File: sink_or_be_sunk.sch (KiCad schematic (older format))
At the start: 57 parts, among them J1 Keypad_Conn, J2 Mux_Conn, J3 Display_Conn, J4 JTAG_Conn, J5 Battery_Conn, J6 USB_B_Micro, J7 Debug_Conn, M1 Motor_DC, Q1 IRLML5203, Q2 2N3704, Q3 2N3704, Q4 Q_PMOS_DGS, SW1 Reset_SW, SW2 SW_DPST, U1 SN74HC151N, U2 LDL1117-SMD, U3 MCP73831-2-OT, U4 MCP608, U5 ESP32-WROOM-32, U6 CY7C65213A-28PVXI

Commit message: finished routing power and programming circuit
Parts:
- removed H2: MountingHole, MountingHole:MountingHole_3.2mm_M3, symbol Mechanical:MountingHole
- removed R? (x2): 20, symbol Device:R
- added H2: ESP_GND_Pad_Hole, MountingHole:MountingHole_2.2mm_M2_DIN965_Pad, symbol Mechanical:MountingHole_Pad
- added H5: Mounting, MountingHole:MountingHole_3.2mm_M3, symbol Mechanical:MountingHole
- added J10, J11, J12, J13, J14, J15, J16, J17, J18, J19, J20, J21, J22, J23, J9: Grid_Conn, Connector_PinSocket_2.54mm:PinSocket_1x06_P2.54mm_Vertical, symbol Connector:Conn_01x06_Female
- added J8: Grid_Conn_LED, Connector_PinSocket_2.54mm:PinSocket_1x07_P2.54mm_Vertical, symbol Connector:Conn_01x07_Female
- added R10, R14, R15, R16, R17, R18, R19, R20, R21, R22, R23, R24, R25, R26, R9: 20, Resistor_SMD:R_0805_2012Metric_Pad1.20x1.40mm_HandSolder, symbol Device:R
- C1, C2, C3, C4: footprint Capacitor_SMD:C_0805_2012Metric_Pad1.18x1.45mm_HandSolder -> Capacitor_THT:CP_Radial_D4.0mm_P2.00mm
- C12: footprint Capacitor_THT:CP_Radial_D8.0mm_P3.50mm -> Capacitor_THT:CP_Radial_D4.0mm_P2.00mm
- C7: value 100uF -> 10uF; footprint Capacitor_THT:CP_Radial_D8.0mm_P3.50mm -> Capacitor_THT:CP_Radial_D4.0mm_P2.00mm
- D2, D5: footprint Diode_THT:D_DO-15_P10.16mm_Horizontal -> Diode_THT:D_A-405_P7.62mm_Horizontal
- H1, H3, H4: value MountingHole -> Mounting
- Q1: value IRLML5203 -> IRL530; symbol Transistor_FET:IRLML5203 -> Device:Q_NMOS_GDS
- Q4: footprint Package_TO_SOT_THT:TO-220-3_Vertical -> Package_TO_SOT_THT:TO-220-3_Horizontal_TabDown
- R13: renamed from R?; footprint Resistor_SMD:R_0805_2012Metric_Pad1.15x1.40mm_HandSolder -> Resistor_SMD:R_0805_2012Metric_Pad1.20x1.40mm_HandSolder
- TP1, TP2: footprint TestPoint:TestPoint_Pad_2.0x2.0mm -> TestPoint:TestPoint_Plated_Hole_D2.0mm
- gave numbers to parts that had none: 1
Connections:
- net DAC_OUT is gone; now on net SPEAKER: U4.2
- net +3V3: now also J10.1 (Pin_1), J11.1 (Pin_1), J12.1 (Pin_1), J13.1 (Pin_1), J14.1 (Pin_1), J15.1 (Pin_1), J16.1 (Pin_1), J17.1 (Pin_1), J18.1 (Pin_1), J19.1 (Pin_1), J20.1 (Pin_1), J21.1 (Pin_1), J22.1 (Pin_1), J23.1 (Pin_1), J8.1 (Pin_1), J9.1 (Pin_1)
- net +BATT: now also SW2.1; no longer SW2.3
- net BOAT_INPUT: now also J10.5 (Pin_5), J11.5 (Pin_5), J12.5 (Pin_5), J13.5 (Pin_5), J14.5 (Pin_5), J15.5 (Pin_5), J16.5 (Pin_5), J17.5 (Pin_5), J18.5 (Pin_5), J19.5 (Pin_5), J20.5 (Pin_5), J21.5 (Pin_5), J22.5 (Pin_5), J23.5 (Pin_5), J8.5 (Pin_5), J9.5 (Pin_5)
- net GND: now also Q1.3 (S), SW2.3, H2.1, J10.6 (Pin_6), J11.6 (Pin_6), J12.6 (Pin_6), J13.6 (Pin_6), J14.6 (Pin_6), J15.6 (Pin_6), J16.6 (Pin_6), J17.6 (Pin_6), J18.6 (Pin_6), J19.6 (Pin_6), J20.6 (Pin_6), J21.6 (Pin_6), J22.6 (Pin_6), J23.6 (Pin_6), J8.7 (Pin_7), J9.6 (Pin_6); no longer Q1.2 (S), SW2.1
- net LCD_CS: now also R19.1; no longer J3.4 (Pin_4)
- net LCD_MOSI: now also R21.1; no longer J3.2 (Pin_2)
- net LCD_SCLK: now also R20.1; no longer J3.3 (Pin_3)
- net LED_OUT: now also J8.6 (Pin_6)
- net MTCK: now also R24.1; no longer J4.3 (Pin_3)
- net MTDI: now also R25.1; no longer J4.2 (Pin_2)
- net MTDO: now also R22.1
- net MTMS: now also R26.1; no longer J4.1 (Pin_1)
- net MUX_COL_SEL0: now also J10.4 (Pin_4), J11.4 (Pin_4), J12.4 (Pin_4), J13.4 (Pin_4), J14.4 (Pin_4), J15.4 (Pin_4), J16.4 (Pin_4), J17.4 (Pin_4), J18.4 (Pin_4), J19.4 (Pin_4), J20.4 (Pin_4), J21.4 (Pin_4), J22.4 (Pin_4), J23.4 (Pin_4), J8.4 (Pin_4), J9.4 (Pin_4)
- net MUX_COL_SEL1: now also J10.2 (Pin_2), J11.2 (Pin_2), J12.2 (Pin_2), J13.2 (Pin_2), J14.2 (Pin_2), J15.2 (Pin_2), J16.2 (Pin_2), J17.2 (Pin_2), J18.2 (Pin_2), J19.2 (Pin_2), J20.2 (Pin_2), J21.2 (Pin_2), J22.2 (Pin_2), J23.2 (Pin_2), J8.2 (Pin_2), J9.2 (Pin_2)
- net MUX_COL_SEL2: now also J10.3 (Pin_3), J11.3 (Pin_3), J12.3 (Pin_3), J13.3 (Pin_3), J14.3 (Pin_3), J15.3 (Pin_3), J16.3 (Pin_3), J17.3 (Pin_3), J18.3 (Pin_3), J19.3 (Pin_3), J20.3 (Pin_3), J21.3 (Pin_3), J22.3 (Pin_3), J23.3 (Pin_3), J8.3 (Pin_3), J9.3 (Pin_3)
- net MUX_ROW0: now also R15.1; no longer J2.4 (Pin_4)
- net MUX_ROW1: now also R14.1; no longer J2.3 (Pin_3)
- net MUX_ROW2: now also R10.1; no longer J2.2 (Pin_2)
- net MUX_ROW3: now also R9.1; no longer J2.1 (Pin_1)
- net MUX_ROW4: now also R16.1; no longer J2.5 (Pin_5)
- net MUX_ROW5: now also R17.1; no longer J2.6 (Pin_6)
- net MUX_ROW6: now also R18.1; no longer J2.7 (Pin_7)
- net MUX_ROW7: now also R23.1; no longer J2.8 (Pin_8)
- net VBUS: no longer C1.1
- net at J4.4 (Pin_4): now also R22.2
- net at SW2.2: now also J5.2 (Pin_2); no longer J5.1 (Pin_1)
- net at SW2.4: now also J5.1 (Pin_1); no longer J5.2 (Pin_2)
- net at D2.2 (A), M1.2 (-): now also Q1.2 (D); no longer Q1.3 (D)
- net Vin: now reaches D5.1 (K), Q4.3 (S), U2.3 (VIN)
- net Vin: now also C1.1
- net SENSOR_VN: no longer names the net of U5.5 (SENSOR_VN)
- net SENSOR_VP: no longer names the net of U5.4 (SENSOR_VP)
- new net: J4.1 (Pin_1), R26.2
- new net: J4.2 (Pin_2), R25.2
- new net: J4.3 (Pin_3), R24.2
- new net: J2.1 (Pin_1), R9.2
- new net: J2.2 (Pin_2), R10.2
- new net: J2.3 (Pin_3), R14.2
- new net: J2.4 (Pin_4), R15.2
- new net: J2.5 (Pin_5), R16.2
- new net: J2.6 (Pin_6), R17.2
- new net: J2.7 (Pin_7), R18.2
- new net: J2.8 (Pin_8), R23.2
- new net: J3.2 (Pin_2), R21.2
- new net: J3.3 (Pin_3), R20.2
- new net: J3.4 (Pin_4), R19.2
- no-connect marks 14 -> 16
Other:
- note added: "R for ESD Protection\n"
- note added: "Speaker/Amplifier"
- note added: "TODO: \n- heat calcs for LDO, MOSFET in Power and filtering section, speaker\n- measure bulk capacitor for diameter(footprints)"
- note removed: "Big Via for pad 39 GND on Esp module for soldering"
- note removed: "Decoupling/Bulk Caps"
- note removed: "Mounting Holes"
- note removed: "R for\nESD Protection\n"
- note removed: "Reset"
- note removed: "TODO: \n- 20 ohm for JTAG, MUX\n- connectors for all 16 grid boards\n- big via for gnd pad on esp\n- heat calcs for LDO, MOSFET in Power and filtering section, speaker\n- test speaker circuit for sound volume"
- note removed: "need headers to Grid PCB"
- moved on the sheet: C1, C10, C11, C12, C2, C3, C4, C5, C6, C7, C8, C9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

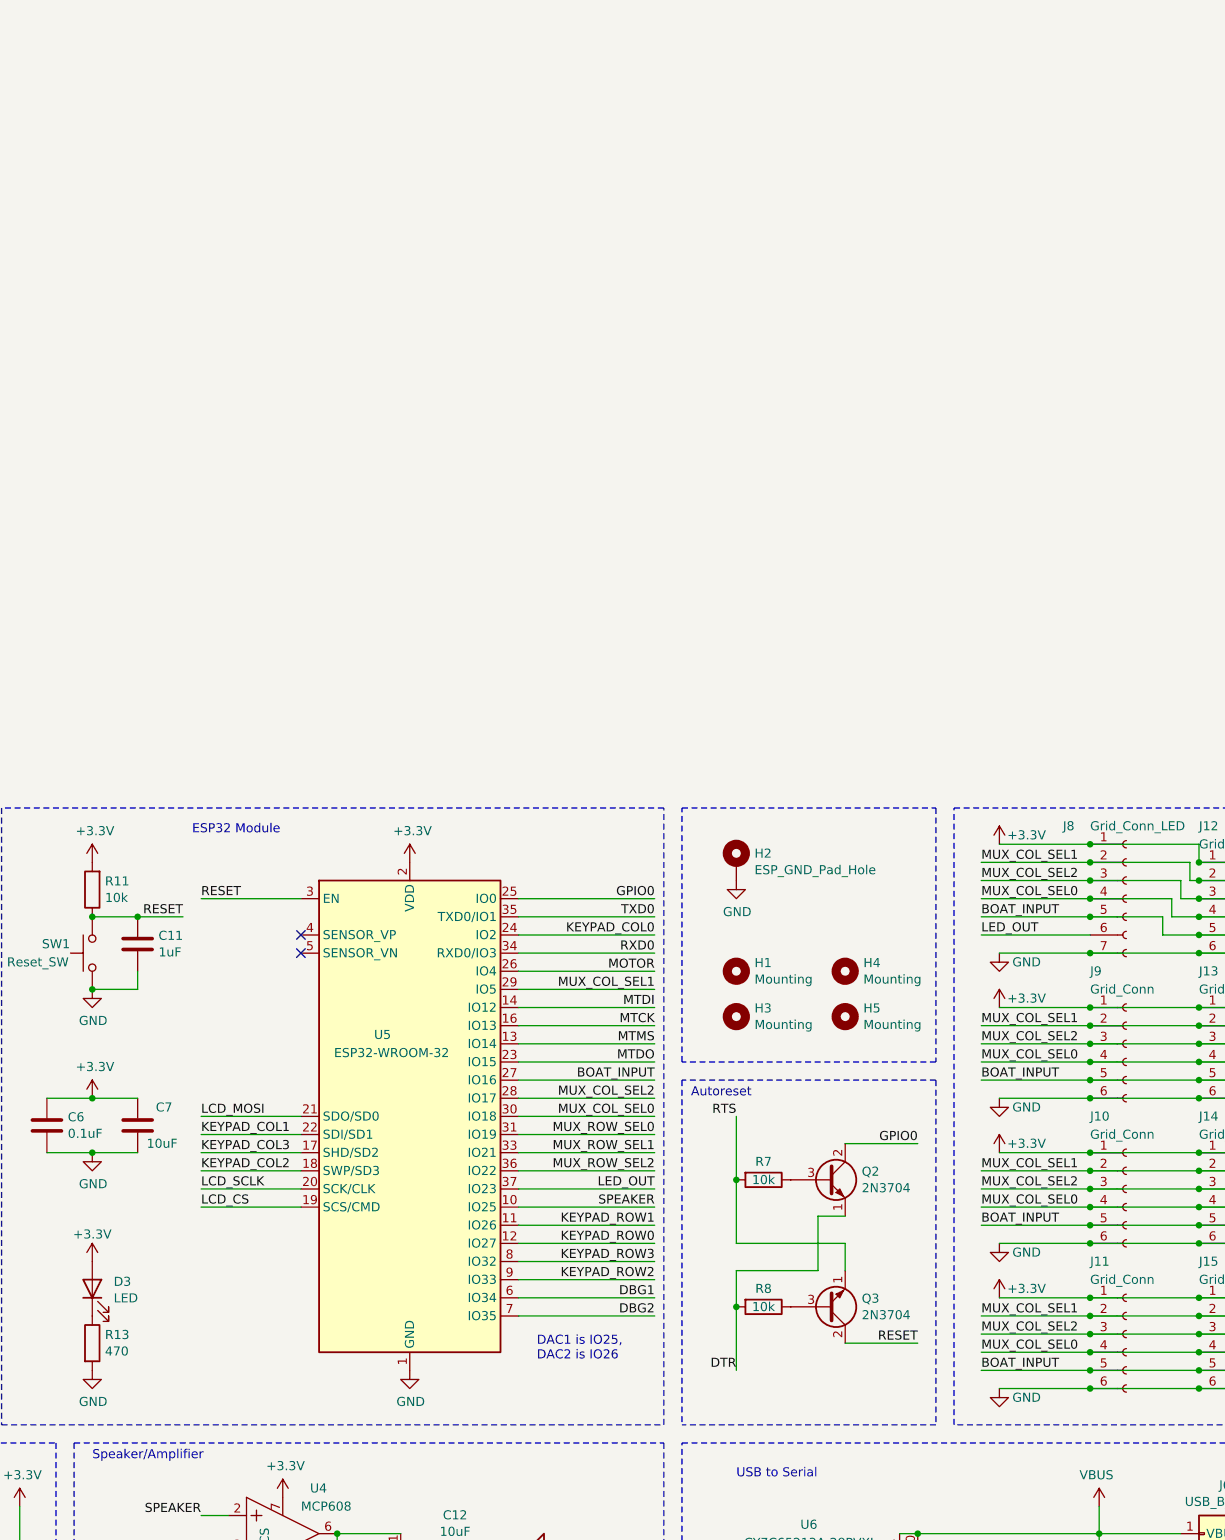
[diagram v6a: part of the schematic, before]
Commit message: finsihed routing mux
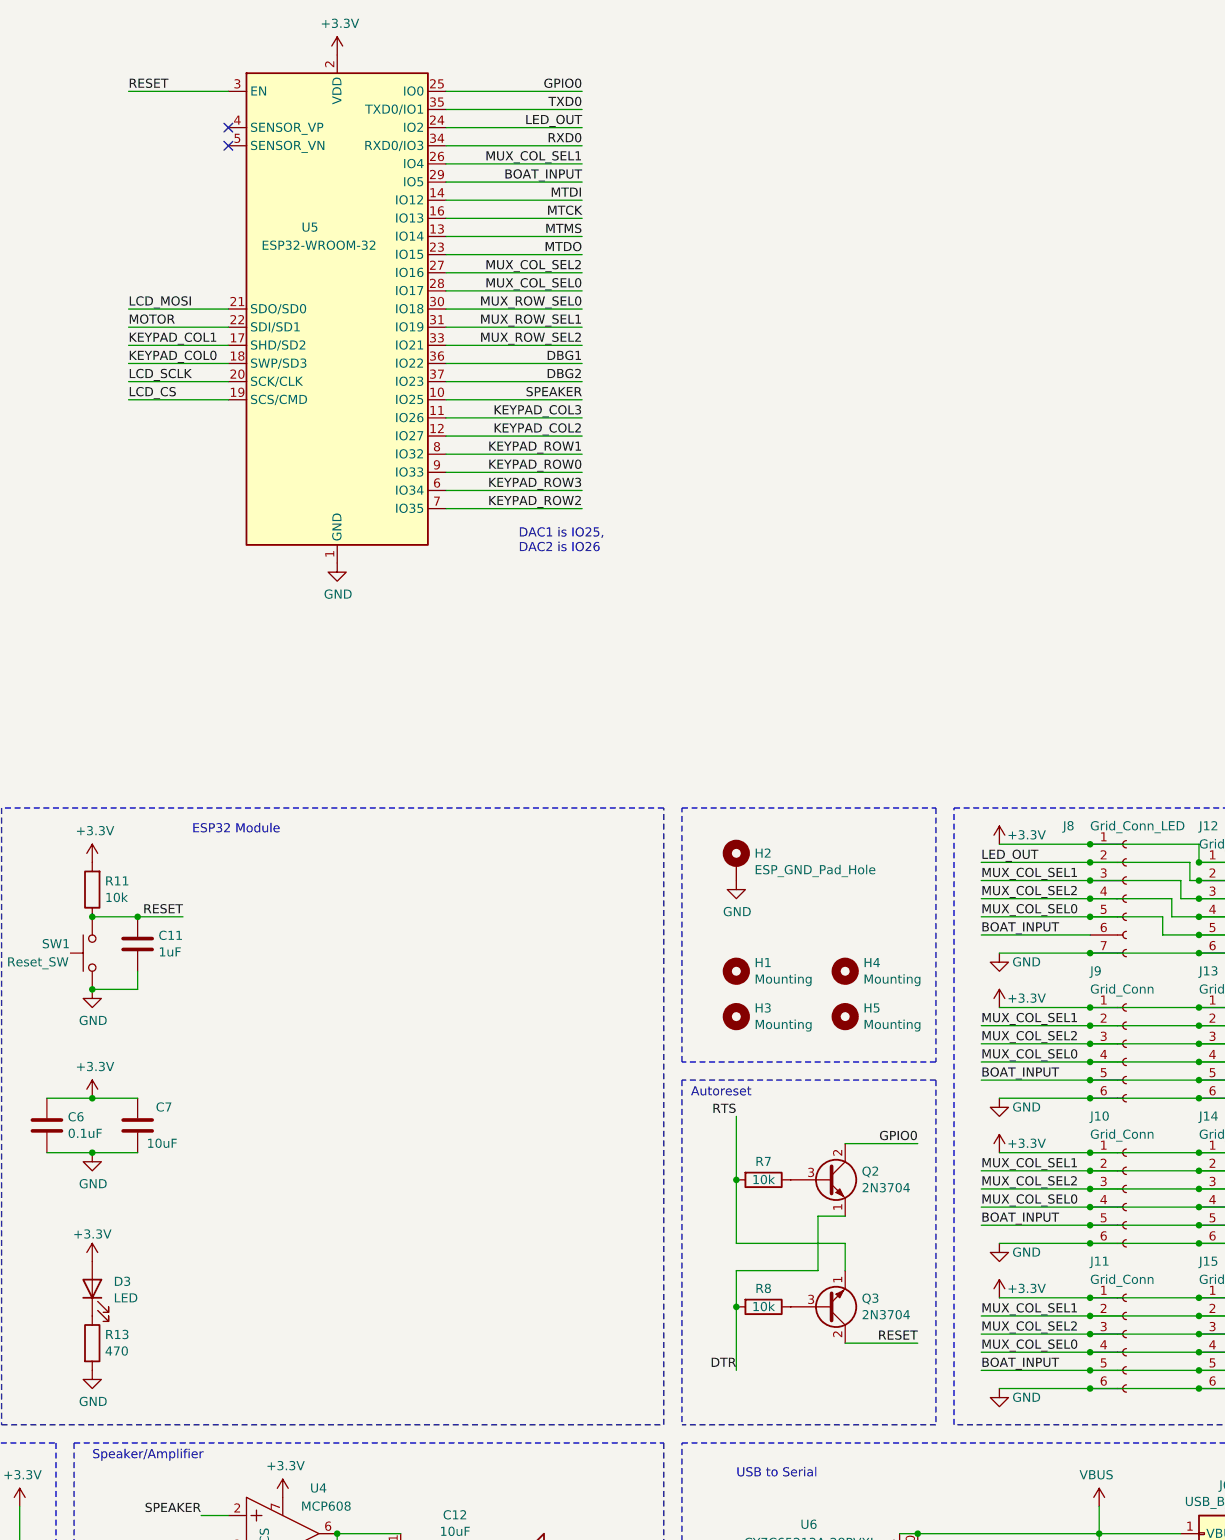
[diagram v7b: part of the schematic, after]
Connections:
- net BOAT_INPUT: now also J8.6 (Pin_6), U5.29 (IO5); no longer J12.5 (Pin_5), J16.5 (Pin_5), J20.5 (Pin_5), J8.5 (Pin_5), U5.27 (IO16)
- net DBG1: now also U5.36 (IO22); no longer U5.6 (IO34)
- net DBG2: now also U5.37 (IO23); no longer U5.7 (IO35)
- net KEYPAD_COL0: now also U5.18 (SWP/SD3); no longer U5.24 (IO2)
- net KEYPAD_COL1: now also U5.17 (SHD/SD2); no longer U5.22 (SDI/SD1)
- net KEYPAD_COL2: now also U5.12 (IO27); no longer U5.18 (SWP/SD3)
- net KEYPAD_COL3: now also U5.11 (IO26); no longer U5.17 (SHD/SD2)
- net KEYPAD_ROW0: now also U5.9 (IO33); no longer U5.12 (IO27)
- net KEYPAD_ROW1: now also U5.8 (IO32); no longer U5.11 (IO26)
- net KEYPAD_ROW2: now also U5.7 (IO35); no longer U5.9 (IO33)
- net KEYPAD_ROW3: now also U5.6 (IO34); no longer U5.8 (IO32)
- net LED_OUT: now also J12.2 (Pin_2), J16.2 (Pin_2), J20.2 (Pin_2), J8.2 (Pin_2), U5.24 (IO2); no longer J8.6 (Pin_6), U5.37 (IO23)
- net MOTOR: now also U5.22 (SDI/SD1); no longer U5.26 (IO4)
- net MUX_COL_SEL0: now also J12.5 (Pin_5), J16.5 (Pin_5), J20.5 (Pin_5), J8.5 (Pin_5), U5.28 (IO17); no longer J12.4 (Pin_4), J16.4 (Pin_4), J20.4 (Pin_4), J8.4 (Pin_4), U5.30 (IO18)
- net MUX_COL_SEL1: now also J12.3 (Pin_3), J16.3 (Pin_3), J20.3 (Pin_3), J8.3 (Pin_3), U5.26 (IO4); no longer J12.2 (Pin_2), J16.2 (Pin_2), J20.2 (Pin_2), J8.2 (Pin_2), U5.29 (IO5)
- net MUX_COL_SEL2: now also J12.4 (Pin_4), J16.4 (Pin_4), J20.4 (Pin_4), J8.4 (Pin_4), U5.27 (IO16); no longer J12.3 (Pin_3), J16.3 (Pin_3), J20.3 (Pin_3), J8.3 (Pin_3), U5.28 (IO17)
- net MUX_ROW_SEL0: now also U5.30 (IO18); no longer U5.31 (IO19)
- net MUX_ROW_SEL1: now also U5.31 (IO19); no longer U5.33 (IO21)
- net MUX_ROW_SEL2: now also U5.33 (IO21); no longer U5.36 (IO22)
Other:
- moved on the sheet: U5

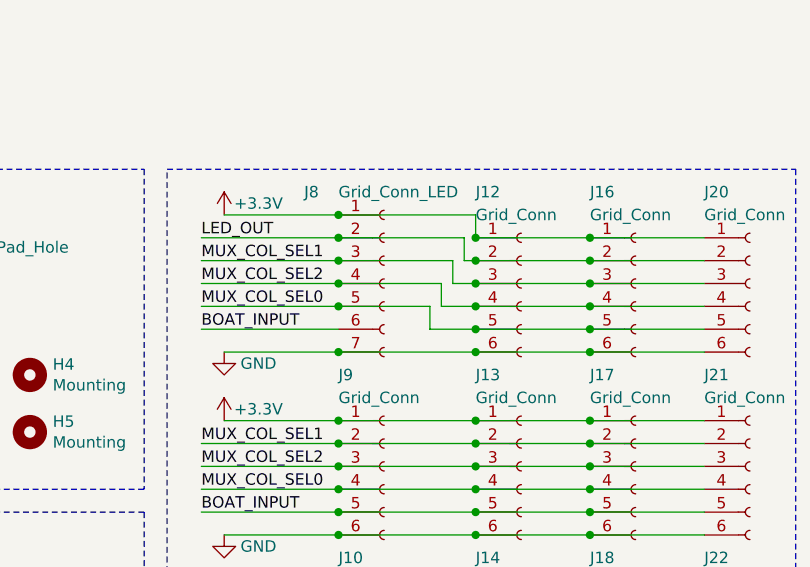
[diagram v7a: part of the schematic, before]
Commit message: fixed error in grid conn sch
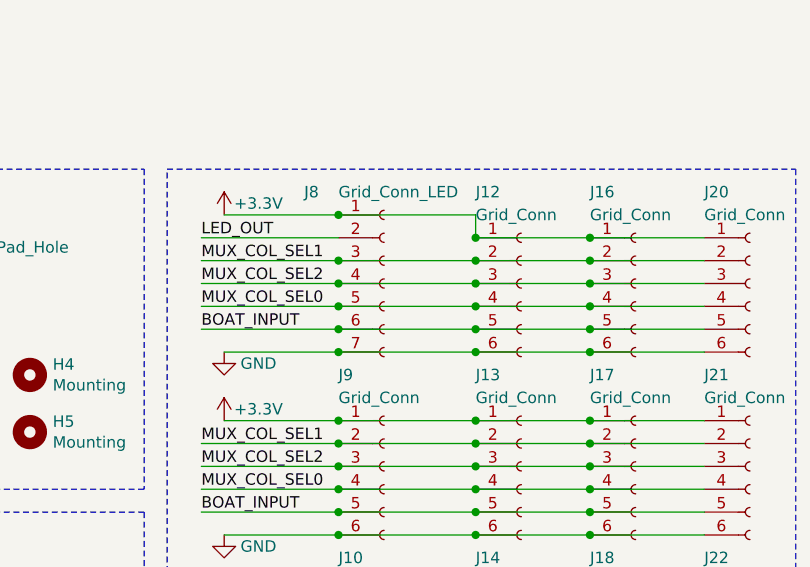
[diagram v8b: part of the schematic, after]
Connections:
- net BOAT_INPUT: now also J12.5 (Pin_5), J16.5 (Pin_5), J20.5 (Pin_5)
- net LED_OUT: no longer J12.2 (Pin_2), J16.2 (Pin_2), J20.2 (Pin_2)
- net MUX_COL_SEL0: now also J12.4 (Pin_4), J16.4 (Pin_4), J20.4 (Pin_4); no longer J12.5 (Pin_5), J16.5 (Pin_5), J20.5 (Pin_5)
- net MUX_COL_SEL1: now also J12.2 (Pin_2), J16.2 (Pin_2), J20.2 (Pin_2); no longer J12.3 (Pin_3), J16.3 (Pin_3), J20.3 (Pin_3)
- net MUX_COL_SEL2: now also J12.3 (Pin_3), J16.3 (Pin_3), J20.3 (Pin_3); no longer J12.4 (Pin_4), J16.4 (Pin_4), J20.4 (Pin_4)
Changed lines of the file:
@@
 Wire Wire Line
 	9200 750  8700 750
-Wire Wire Line
-	9750 950  9750 850
-Wire Wire Line
-	9750 850  9200 850
-Wire Wire Line
-	9750 950  9800 950
 Connection ~ 9800 950
 Wire Wire Line
@@
 Wire Wire Line
 	10800 1050 10300 1050
-Wire Wire Line
-	9700 1050 9700 950
-Wire Wire Line
-	9700 950  9200 950
-Connection ~ 9800 1050
-Wire Wire Line
-	9800 1050 9700 1050
 Connection ~ 10300 1050
 Wire Wire Line
@@
 Wire Wire Line
 	10800 1150 10300 1150
-Wire Wire Line
-	9650 1150 9650 1050
-Wire Wire Line
-	9650 1050 9200 1050
-Connection ~ 9800 1150
-Wire Wire Line
-	9800 1150 9650 1150
 Connection ~ 10300 1150
 Wire Wire Line
@@
 Wire Wire Line
 	10800 1250 10300 1250
-Wire Wire Line
-	9600 1250 9600 1150
-Wire Wire Line
-	9600 1150 9200 1150
 Connection ~ 9800 1250
-Wire Wire Line
-	9800 1250 9600 1250
 Connection ~ 10300 1250
 Wire Wire Line
@@
 Wire Wire Line
 	6400 -3000 5650 -3000
-Connection ~ 9200 850
+Wire Wire Line
+	9200 950  9800 950
 Connection ~ 9200 950
+Wire Wire Line
+	9200 1050 9800 1050
 Connection ~ 9200 1050
+Connection ~ 9800 1050
+Wire Wire Line
+	9800 1150 9200 1150
+Connection ~ 9800 1150
 Connection ~ 9200 1150
+Wire Wire Line
+	9200 1250 9800 1250
+Connection ~ 9200 1250
 $EndSCHEMATC
